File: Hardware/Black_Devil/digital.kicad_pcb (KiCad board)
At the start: 2 copper layers, 160 x 100 mm, 99 parts, among them J101 L1, J102 N, J103 UART, J104 OLED, J105 Encoder, J106 Up2Stream, J107 ICSP, J108 Klinke_Right, J109 Klinke_Links, J110 Cinch_Right, J111 Cinch_Left, J112 Left, J113 Right, J114 VU-Meter, J115 Up2Stream, K101 G6K-2, K102 G6K-2, K103 G6K-2, Q101 BSS138, Q102 BSS138, Q103 BSS138, Q104 BSS138, Q105 BSS138, Q106 BSS138, Q107 BSS138, SW101 RotaryEncoder_Switch, U101 ATmega328P-A, U102 L7805, U103 L7805, U104 AP1117-33, Y101 16MHz

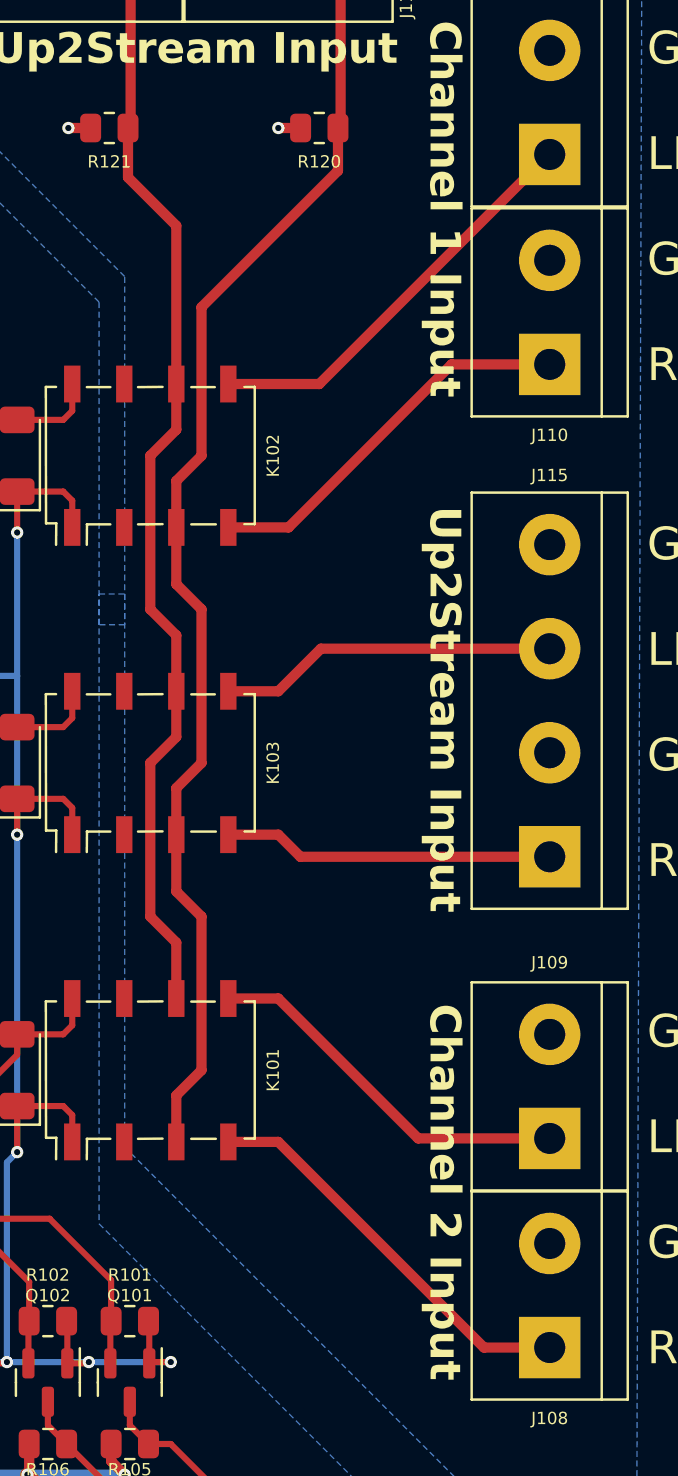
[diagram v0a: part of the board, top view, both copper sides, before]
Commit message: rounding tracks on audio side
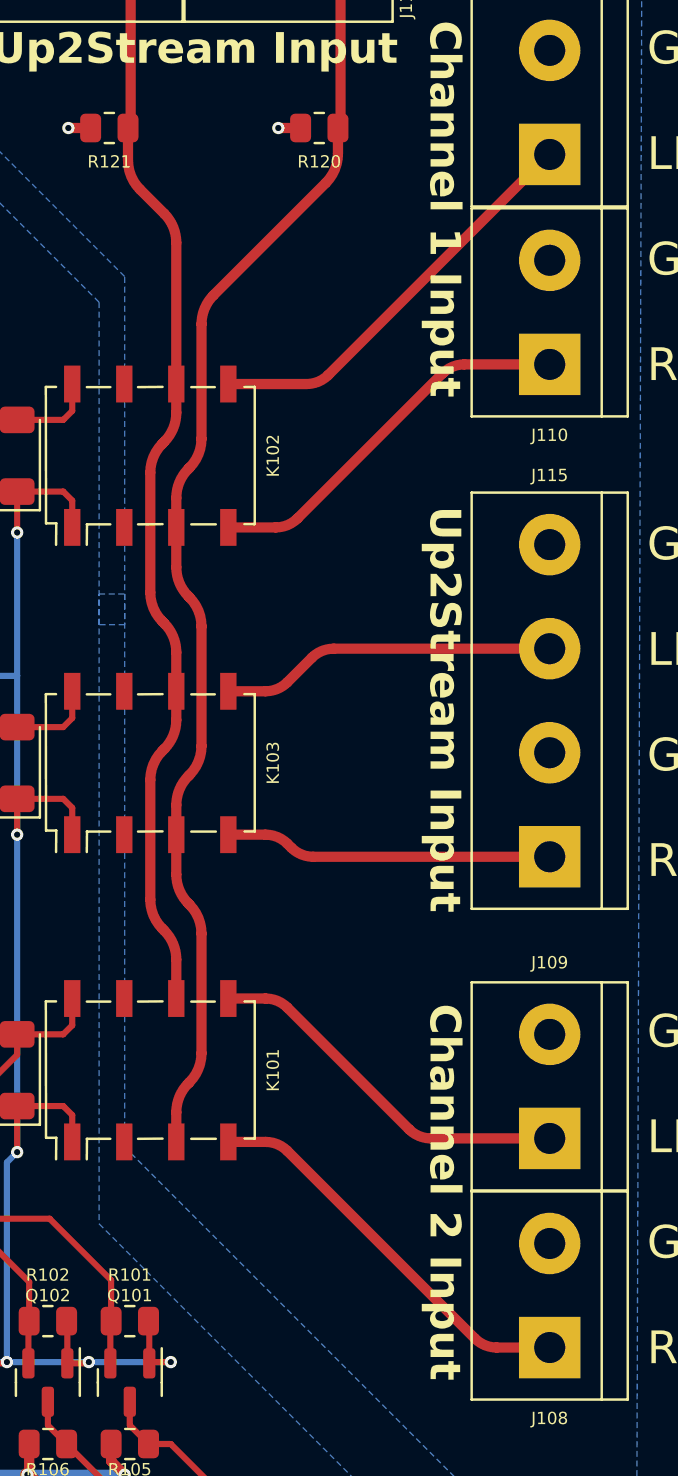
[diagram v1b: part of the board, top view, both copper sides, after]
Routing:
- net /Right: track 63.9 -> 62.7 mm
- net /Left: track 54.6 -> 53.7 mm

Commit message: Reviews
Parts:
- removed Q101, Q102: BSS138, Package_TO_SOT_SMD:SOT-23
- removed R105, R106: 4k7, Resistor_SMD:R_0805_2012Metric
- removed the REF** at (191.0, 49.0)
- removed the REF** at (39.0, 141.0)
- removed the REF** at (113.0, 49.0)
- removed the REF** at (113.0, 141.0)
- removed the REF** at (39.0, 49.0)
- removed the REF** at (191.0, 141.0)
- removed TP104: 9V, TestPoint:TestPoint_Loop_D2.50mm_Drill1.0mm
- removed TP105: GND, TestPoint:TestPoint_Loop_D2.50mm_Drill1.0mm
- added C121: 470µ, Capacitor_THT:CP_Radial_D10.0mm_P5.00mm, F.Cu at (107.6, 105.8)
- added C122: 470µ, Capacitor_THT:CP_Radial_D10.0mm_P5.00mm, F.Cu at (107.6, 116.2)
- added C123: 470µ, Capacitor_THT:CP_Radial_D10.0mm_P5.00mm, F.Cu at (101.6, 105.8)
- added C124: 470µ, Capacitor_THT:CP_Radial_D10.0mm_P5.00mm, F.Cu at (101.6, 116.2)
- added C125: 1µ, Capacitor_SMD:C_0805_2012Metric, F.Cu at (143.0, 89.2)
- added C126: 1µ, Capacitor_SMD:C_0805_2012Metric, F.Cu at (139.4, 89.2)
- added C127: 100n, Capacitor_SMD:C_0805_2012Metric, F.Cu at (133.2, 68.5)
- added C128: 100n, Capacitor_SMD:C_0805_2012Metric, F.Cu at (131.8, 59.2)
- added D108: 1N4004, Diode_THT:D_DO-41_SOD81_P10.16mm_Horizontal, F.Cu at (108.0, 123.4)
- added D109: 1N4004, Diode_THT:D_DO-41_SOD81_P10.16mm_Horizontal, F.Cu at (111.2, 133.6)
- added D110: 1N4004, Diode_THT:D_DO-41_SOD81_P10.16mm_Horizontal, F.Cu at (101.5, 123.4)
- added D111: 1N4004, Diode_THT:D_DO-41_SOD81_P10.16mm_Horizontal, F.Cu at (98.2, 133.6)
- added G***: LOGO, TheBrutzlers_Lib:approved_theBrutzler, F.Cu at (147.8, 121.1)
- added REF**: MountingHole_3.2mm_M3_DIN965, MountingHole:MountingHole_3.2mm_M3_DIN965, F.Cu at (192.0, 48.0)
- added REF**: MountingHole_3.2mm_M3_DIN965, MountingHole:MountingHole_3.2mm_M3_DIN965, F.Cu at (115.0, 142.0)
- added REF**: MountingHole_3.2mm_M3_DIN965, MountingHole:MountingHole_3.2mm_M3_DIN965, F.Cu at (115.0, 48.0)
- added REF**: MountingHole_3.2mm_M3_DIN965, MountingHole:MountingHole_3.2mm_M3_DIN965, F.Cu at (192.0, 142.0)
- added REF**: MountingHole_3.2mm_M3_DIN965, MountingHole:MountingHole_3.2mm_M3_DIN965, F.Cu at (38.0, 142.0)
- added REF**: MountingHole_3.2mm_M3_DIN965, MountingHole:MountingHole_3.2mm_M3_DIN965, F.Cu at (38.0, 48.0)
- added TH101: Thermistor_NTC, Connector_PinHeader_2.54mm:PinHeader_1x02_P2.54mm_Vertical, F.Cu at (142.0, 79.5)
- added TH102: Thermistor_NTC, Connector_PinHeader_2.54mm:PinHeader_1x02_P2.54mm_Vertical, F.Cu at (138.2, 79.5)
- added U105: ADuM1201AR, Package_SO:SOIC-8_3.9x4.9mm_P1.27mm, F.Cu at (136.2, 62.2)
- J103: value UART -> OLED; footprint Connector_JST:JST_XH_B3B-XH-A_1x03_P2.50mm_Vertical -> Connector_JST:JST_XH_B4B-XH-A_1x04_P2.50mm_Vertical
- moved G*** 134.5 mm to (154.2, 54.2)
- moved REF** 134.4 mm to (164.5, 54.5)
- moved J103 94.3 mm to (132.2, 53.8), turned to 0 degrees
- moved SW101 90.7 mm to (163.5, 140.0), turned to -90 degrees
- moved J105 58.0 mm to (160.5, 127.0), turned to 0 degrees
- moved R114 48.5 mm to (153.6, 70.4), turned to 0 degrees
- moved REF** 47.1 mm to (53.2, 57.5)
- moved R117 46.2 mm to (153.6, 72.4), turned to 180 degrees
- moved R116 45.8 mm to (157.1, 70.4), turned to 0 degrees
- moved R115 43.5 mm to (160.6, 70.4), turned to 0 degrees
- moved R119 43.4 mm to (157.1, 72.4), turned to 180 degrees
- moved Q105 42.9 mm to (153.6, 75.4), turned to -90 degrees
- moved R118 40.9 mm to (160.6, 72.4), turned to 180 degrees
- moved R101 40.5 mm to (143.0, 91.2)
- moved R102 40.3 mm to (139.4, 91.2)
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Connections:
- C101 pad 1: +12V -> +12VA
- C101 pad 2: GND -> GND1
- C102 pad 1: +12V -> +12VA
- C102 pad 2: GND -> GND1
- C103 pad 1: +5V -> +5VA
- C103 pad 2: GND -> GND1
- C104 pad 1: +5V -> +5VA
- C104 pad 2: GND -> GND1
- C108 pad 1: +12V -> +12VA
- C108 pad 2: GND -> GND1
- C109 pad 1: +12V -> +12VA
- C109 pad 2: GND -> GND1
- C110 pad 1: +12V -> +12VA
- C110 pad 2: GND -> GND1
- C113 pad 1: +12V -> +12VA
- C113 pad 2: GND -> GND1
- C114 pad 1: +5VA -> +5V
- C115 pad 1: +5VA -> +5V
- C116 pad 1: +5VA -> +5V
- C117 pad 1: +5VA -> +5V
- C120 pad 1: +5VA -> +5V
- D101 pad 1: +12V -> +12VA
- D102 pad 2: GND -> GND1
- D103 pad 1: +12V -> +12VA
- D104 pad 2: GND -> GND1
- D105 pad 1: +5VA -> +5V
- D106 pad 1: +5VA -> +5V
- D107 pad 1: +5VA -> +5V
- J103 pad 1: GND -> Net-(J103-Pin_1)
- J105 pad 2: +5VA -> +5V
- J106 pad 1: +5V -> +5VA
- J106 pad 2: GND -> GND1
- J107 pad 2: +5VA -> +5V
- J108 pad 2: GND -> /Sig_GND
- J109 pad 2: GND -> /Sig_GND
- J110 pad 2: GND -> /Sig_GND
- J111 pad 2: GND -> /Sig_GND
- J112 pad 2: GND -> /Sig_GND
- J113 pad 2: GND -> /Sig_GND
- J114 pad 1: +5VA -> +5V
- J115 pad 2: GND -> /Sig_GND
- J115 pad 4: GND -> /Sig_GND
- K101 pad 1: +5VA -> +5V
- K102 pad 1: +5VA -> +5V
- K103 pad 1: +5VA -> +5V
- Q103 pad 1: +5VA -> +3V3
- Q103 pad 2: SCL -> Net-(J104-Pin_3)
- Q103 pad 3: Net-(J104-Pin_3) -> SCL
- Q104 pad 1: +5VA -> +3V3
- Q104 pad 2: SDA -> Net-(J104-Pin_4)
- Q104 pad 3: Net-(J104-Pin_4) -> SDA
- R101 pad 1: +5VA -> +5V
- R101 pad 2: RxD -> NTC1
- R102 pad 1: +5VA -> NTC2
- R102 pad 2: TxD -> +5V
- R103 pad 1: +5VA -> +5V
- R104 pad 1: +5VA -> +5V
- R110 pad 1: +5VA -> +5V
- R111 pad 1: +5VA -> +5V
- R112 pad 1: +5VA -> +5V
- R113 pad 1: +5VA -> +5V
- R120 pad 2: GND -> /Sig_GND
- R121 pad 2: GND -> /Sig_GND
- TR101 pad 5: Net-(D103-A) -> Net-(D110-A)
- TR101 pad 6: Net-(D101-A) -> Net-(D108-A)
- U101 pad 18: +5VA -> +5V
- U101 pad 20: +5VA -> +5V
- U101 pad 23: unconnected-(U101-PC0-Pad23) -> NTC1
- U101 pad 24: unconnected-(U101-PC1-Pad24) -> NTC2
- U101 pad 4: +5VA -> +5V
- U101 pad 6: +5VA -> +5V
- U102 pad 1: +12V -> +12VA
- U102 pad 2: GND -> GND1
- U102 pad 3: +5V -> +5VA
- U103 pad 3: +5VA -> +5V
- U104 pad 3: +5VA -> +5V
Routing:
- net +5V: track 21.3 -> 284.2 mm, vias 0 -> 11
- net +5VA: track 266.3 -> 30.5 mm, vias 9 -> 0
- net +12V: track 107.9 -> 0.00 mm
- net Net-(D108-A): track 0.00 -> 45.2 mm
- net RST: track 14.0 -> 43.7 mm
- net Net-(D105-A): track 12.0 -> 40.7 mm
- net Net-(D106-A): track 35.0 -> 8.56 mm
- net RxD: track 66.8 -> 41.4 mm
- net MISO: track 18.5 -> 39.6 mm, vias 2 -> 0
- net Net-(D110-A): track 0.00 -> 21.0 mm
- net NTC2: track 0.00 -> 19.5 mm
- net MOSI: track 12.8 -> 31.8 mm, vias 2 -> 0
- net TxD: track 60.6 -> 41.9 mm
- net NTC1: track 0.00 -> 18.2 mm
- net Net-(D103-A): track 66.8 -> 84.1 mm
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- added copper zone on F.Cu, net +12V
- added copper zone on F.Cu, net +12VA
- added copper zone on B.Cu, net /Sig_GND
- added copper zone on B.Cu, net GND1
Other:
- board text added: "3V3 TxD RxD GND"
- board text added: "Audio Output"
- board text removed: "12V"
- board text removed: "GND"
- board text removed: "TxD RxD GND"

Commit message: Reviews, Gerber Plots and Overview Update
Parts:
- added TP104: TestPoint, TestPoint:TestPoint_Loop_D2.50mm_Drill1.0mm, F.Cu at (131.0, 131.2)
- added TP105: TestPoint, TestPoint:TestPoint_Loop_D2.50mm_Drill1.0mm, F.Cu at (131.0, 127.2)
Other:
- board text added: "5V GND"
